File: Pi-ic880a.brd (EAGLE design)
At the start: 87 x 96 mm, 28 parts, among them U1 IC880A, U2 BR24G32-3, U3 DS3231SN

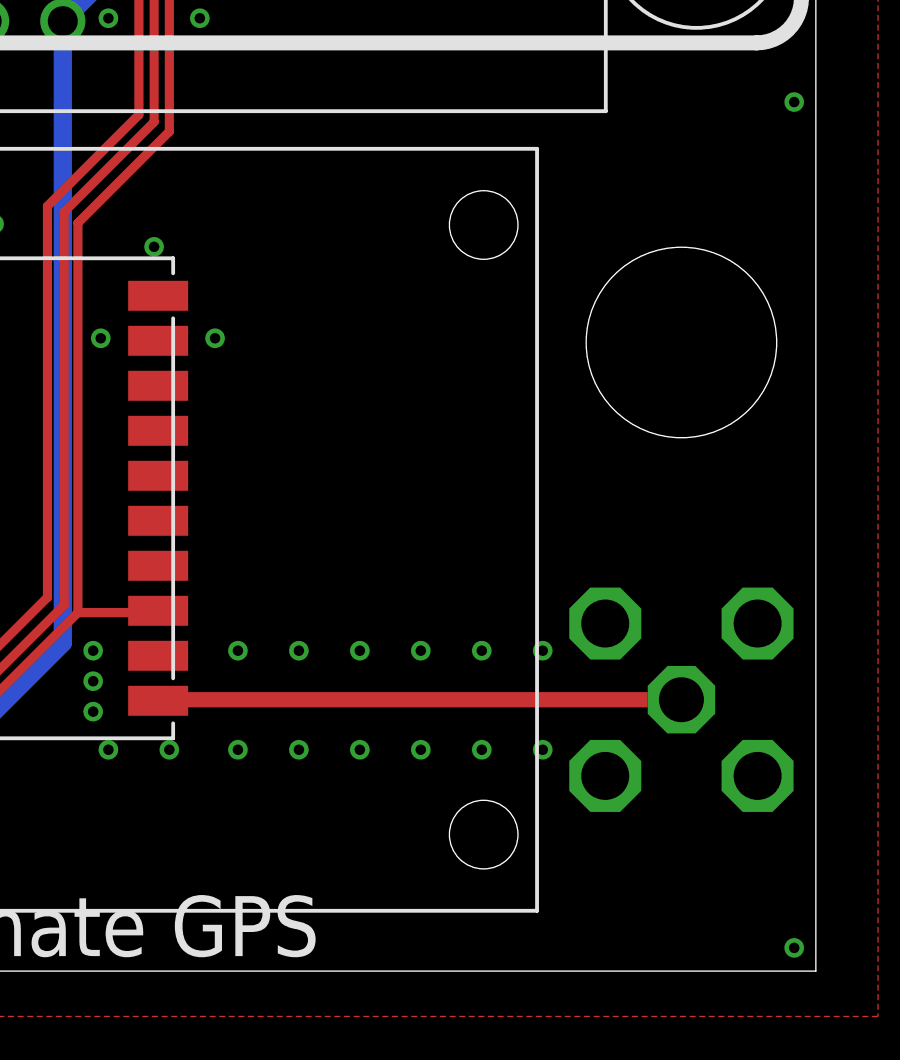
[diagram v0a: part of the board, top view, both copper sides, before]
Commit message: Mounting holes for adafruit module now corrected
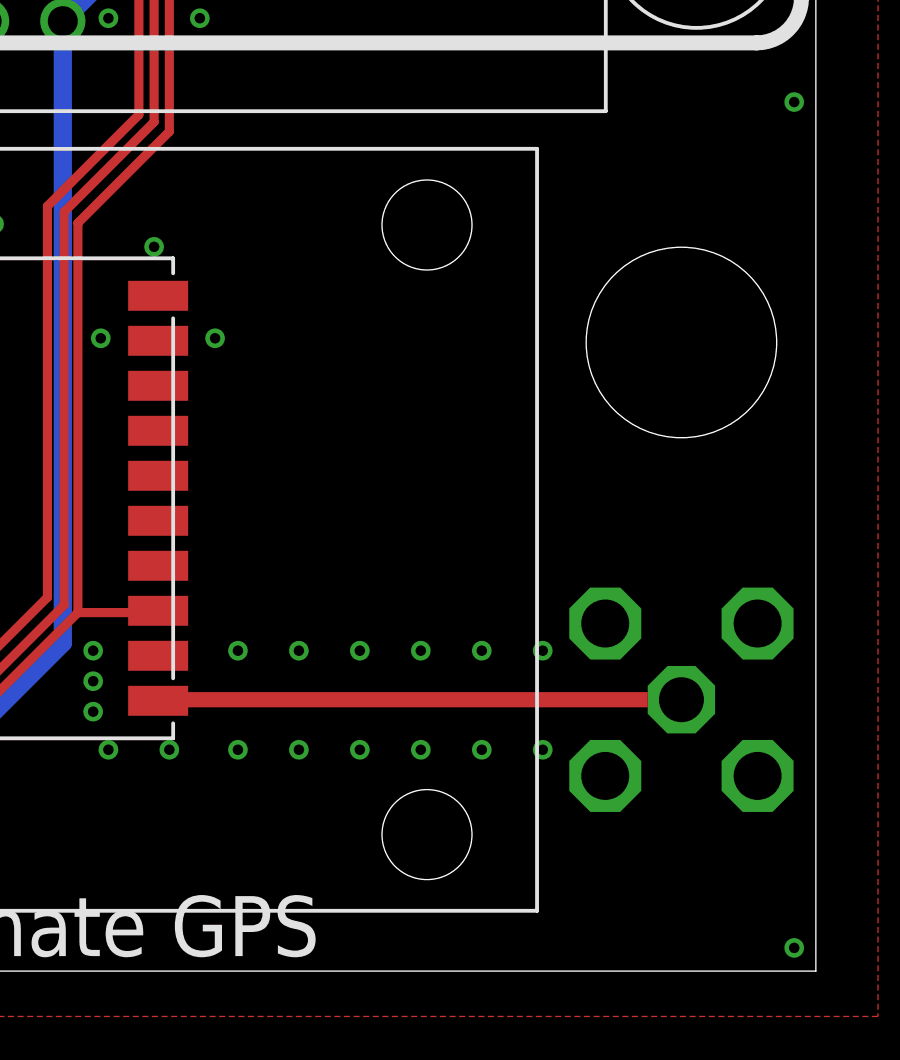
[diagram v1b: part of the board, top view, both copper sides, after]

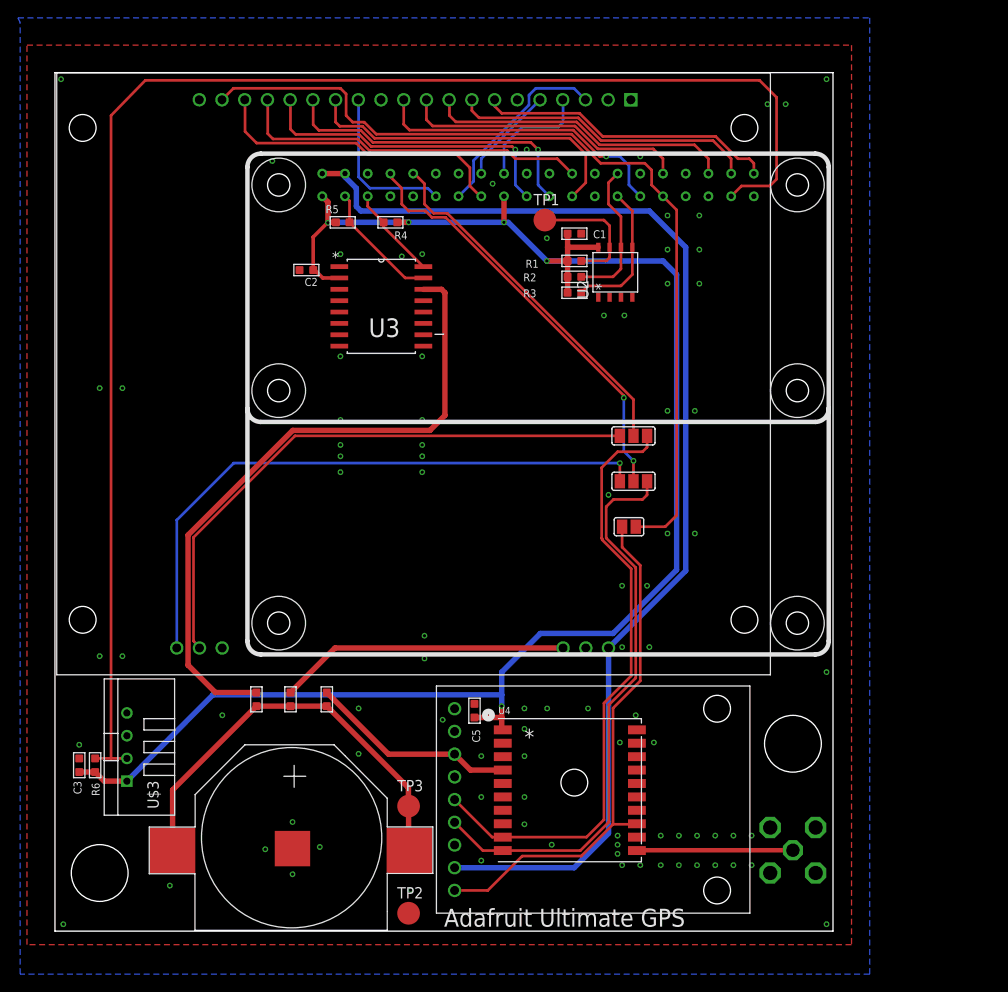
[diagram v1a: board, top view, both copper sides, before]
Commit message: Layout tweaks
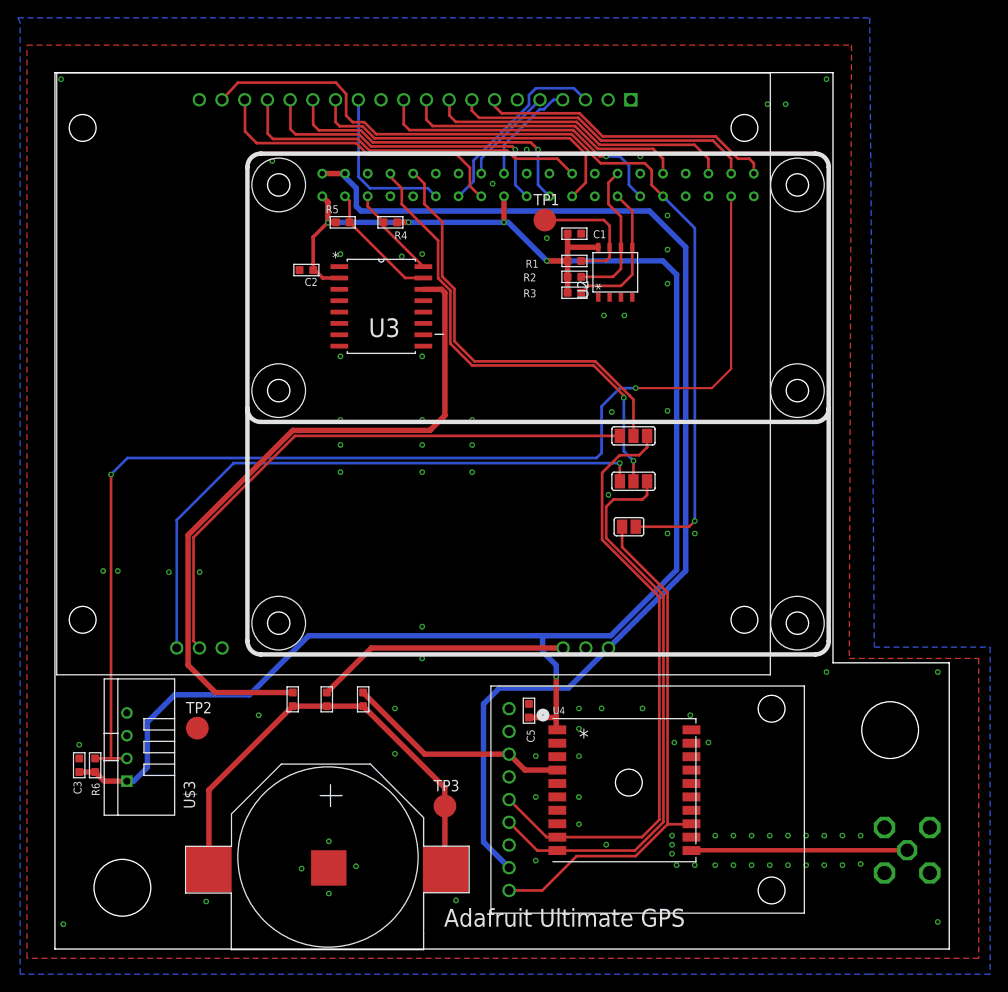
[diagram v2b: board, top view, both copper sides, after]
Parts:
- moved TP2 31.4 mm to (-5.08, -8.30)
- moved U$2 12.8 mm to (74.3, -22.0)
- moved GPS1 6.10 mm to (45.3, -16.3)
- moved C5 6.10 mm to (32.0, -6.35)
- moved U4 6.10 mm to (42.7, -15.2)
- moved U$1 4.60 mm to (7.92, -15.3)
- moved R7 4.06 mm to (5.59, -5.08)
- moved R8 4.06 mm to (13.5, -5.08)
- moved R9 4.06 mm to (9.40, -5.08)
- moved TP3 4.06 mm to (22.6, -17.0)
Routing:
- net DHT22: track 167.3 -> 131.9 mm, vias 0 -> 2
- net +3V3: track 190.0 -> 198.7 mm
- net PI_RXD: track 40.5 -> 47.5 mm
- net GPS_ANT: track 17.5 -> 24.1 mm
- net PI_TXD: track 47.8 -> 53.7 mm
- net VBAT: track 47.9 -> 52.1 mm
- net VBAT_IC880: track 32.5 -> 28.5 mm
- net VBAT_RTC: track 74.0 -> 78.1 mm
- net PPS: track 98.6 -> 102.5 mm, vias 0 -> 1
- net +5V: track 133.4 -> 129.9 mm
- net VBAT_GPS: track 23.3 -> 25.3 mm
- net SP_VALID: track 13.4 -> 11.9 mm
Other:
- board size 87 x 96 mm -> 100 x 98 mm

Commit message: V2 about ready to go
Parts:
- C3: value 100pf -> 100nf
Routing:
- net PPS: track 102.5 -> 103.6 mm
- net ADA_TXD: track 69.0 -> 70.0 mm
- net SX1301_RST: track 18.2 -> 17.4 mm
- net SX1301_GPIO0: track 33.5 -> 32.8 mm

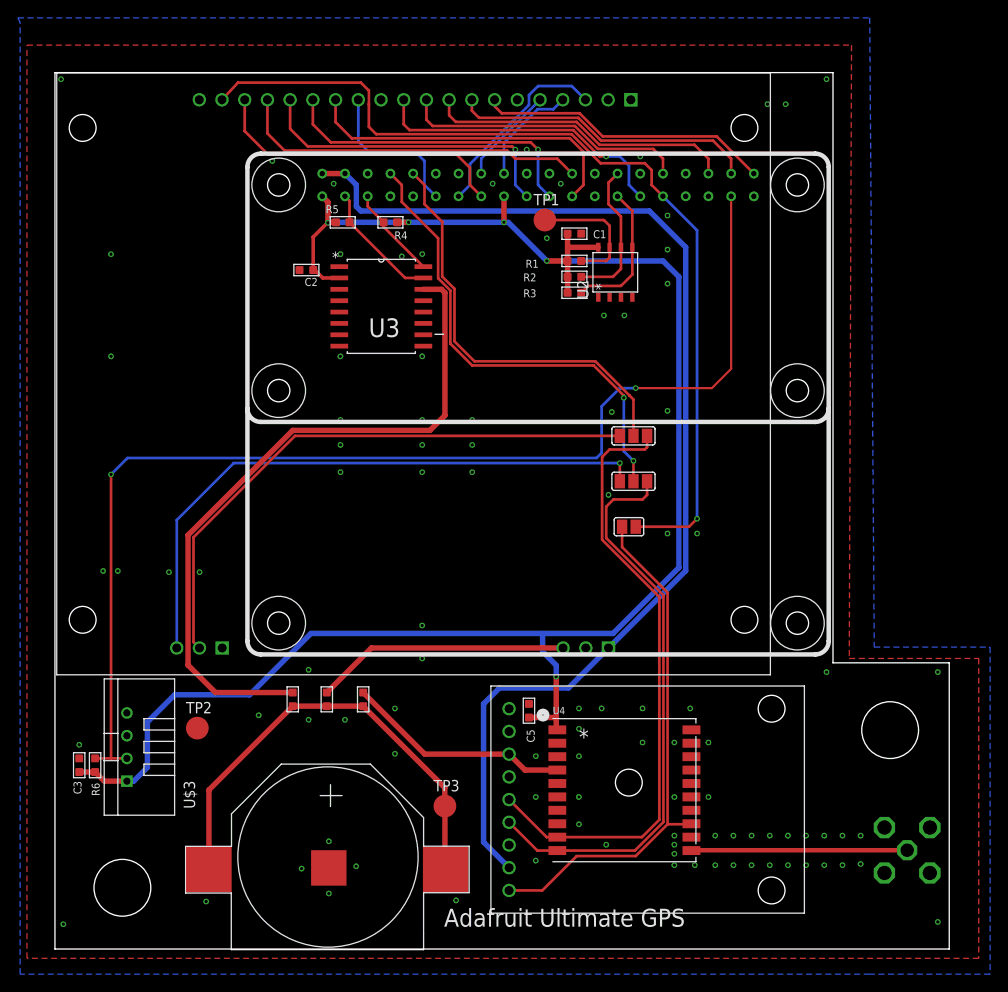
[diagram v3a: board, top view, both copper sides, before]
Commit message: DC jack added Now called Pi-CoT smd GPS moved closer to ant holes for Pi connector now bigger
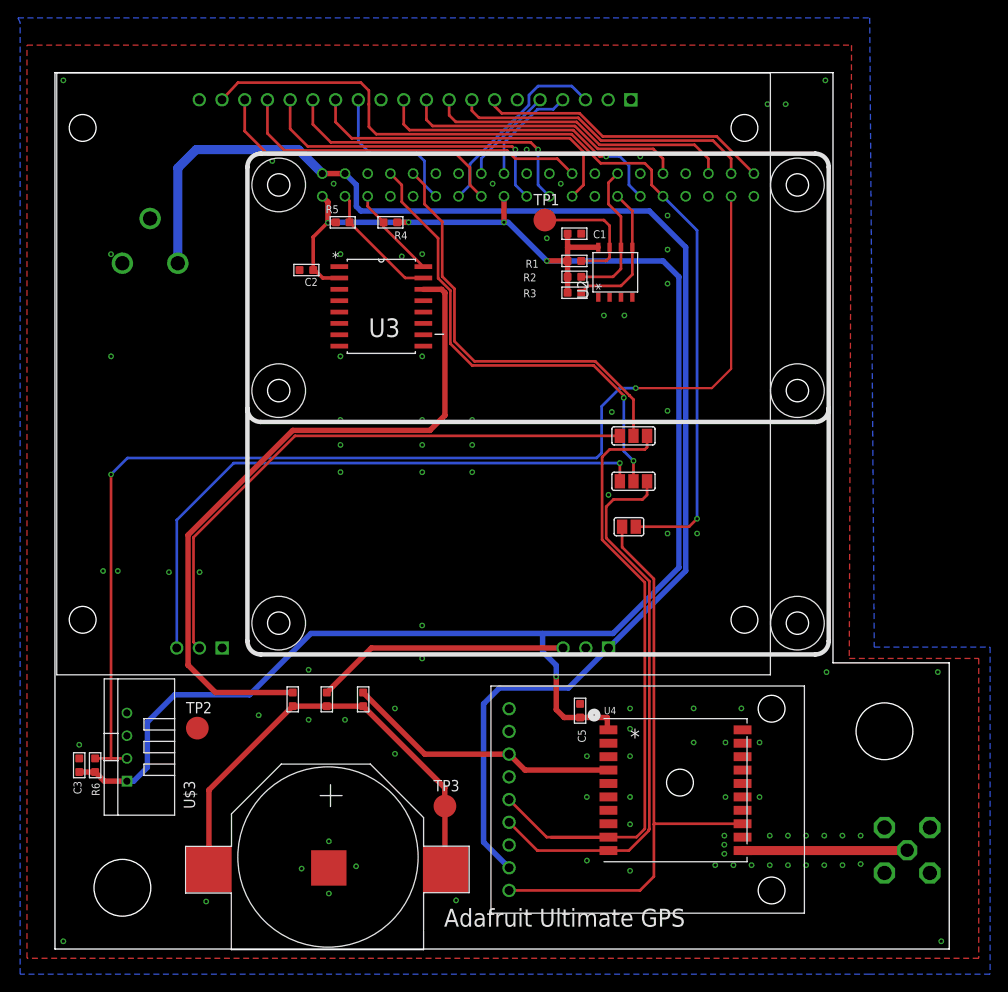
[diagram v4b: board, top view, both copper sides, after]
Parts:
- added J1: FC681465P, farnell-parts:FC681465P
- moved C5 5.72 mm to (37.7, -6.35)
- moved U4 5.72 mm to (48.4, -15.2)
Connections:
- net +5V: now also J1.1
- net GND: now also J1.3
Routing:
- net +5V: track 129.9 -> 158.7 mm
- net ADA_PPS: track 59.7 -> 67.4 mm
- net VBAT_GPS: track 25.3 -> 31.0 mm
- net GPS_ANT: track 24.1 -> 18.4 mm
- net ADA_TXD: track 70.0 -> 74.0 mm
- net +3V3: track 199.2 -> 201.4 mm
- net ADA_RXD: track 64.4 -> 62.7 mm
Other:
- board text added: "5V DC"
- board text added: "Pi-CoT"
